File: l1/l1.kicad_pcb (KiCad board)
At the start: 2 copper layers, 113 parts, among them J201 Conn_01x10, SW201 SW_SPDT, U201 STM32F103CBTX, U202 CD74HC4067SM, U203 CD74HC4067SM, U204 TPS22917x, U205 ILD8150, Y201 8Mhz

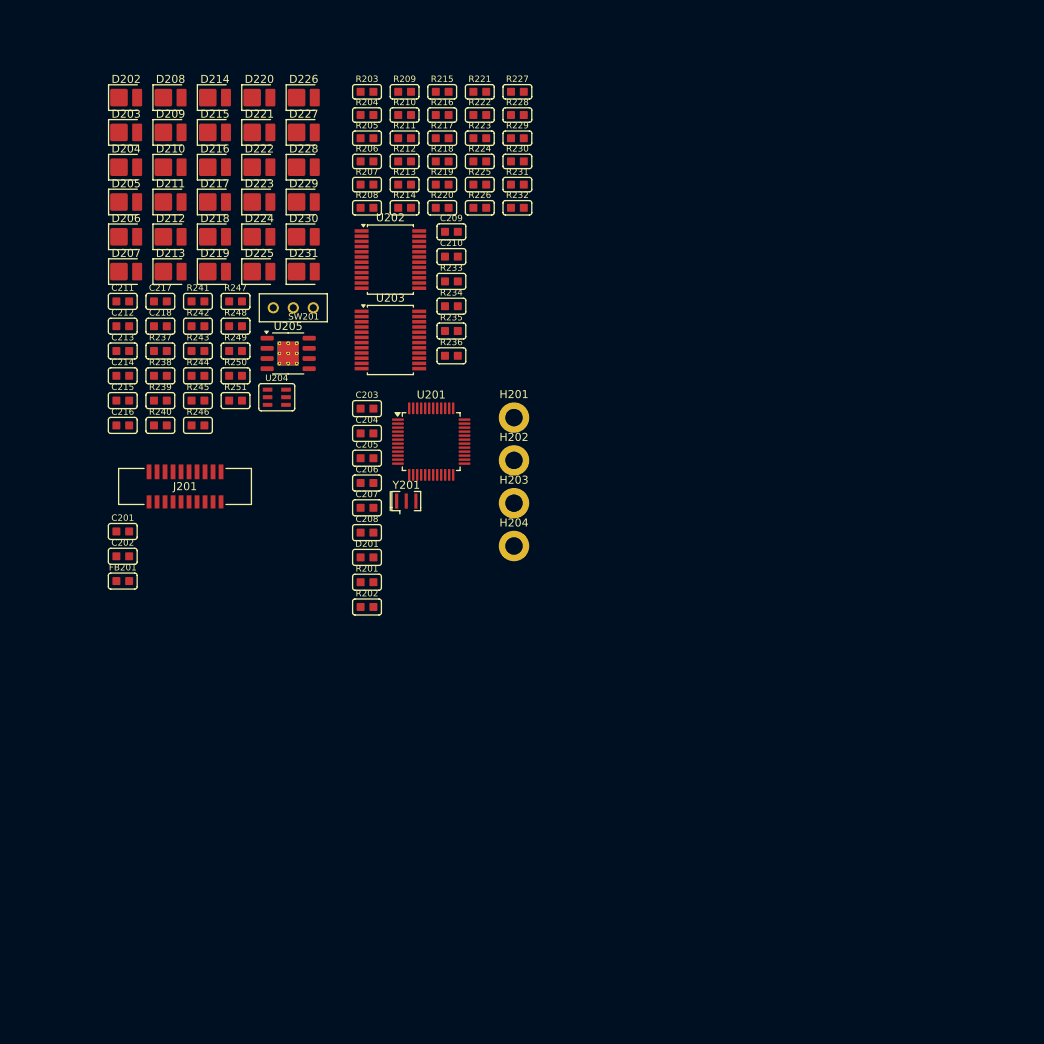
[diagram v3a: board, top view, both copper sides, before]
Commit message: Going to move to VNH
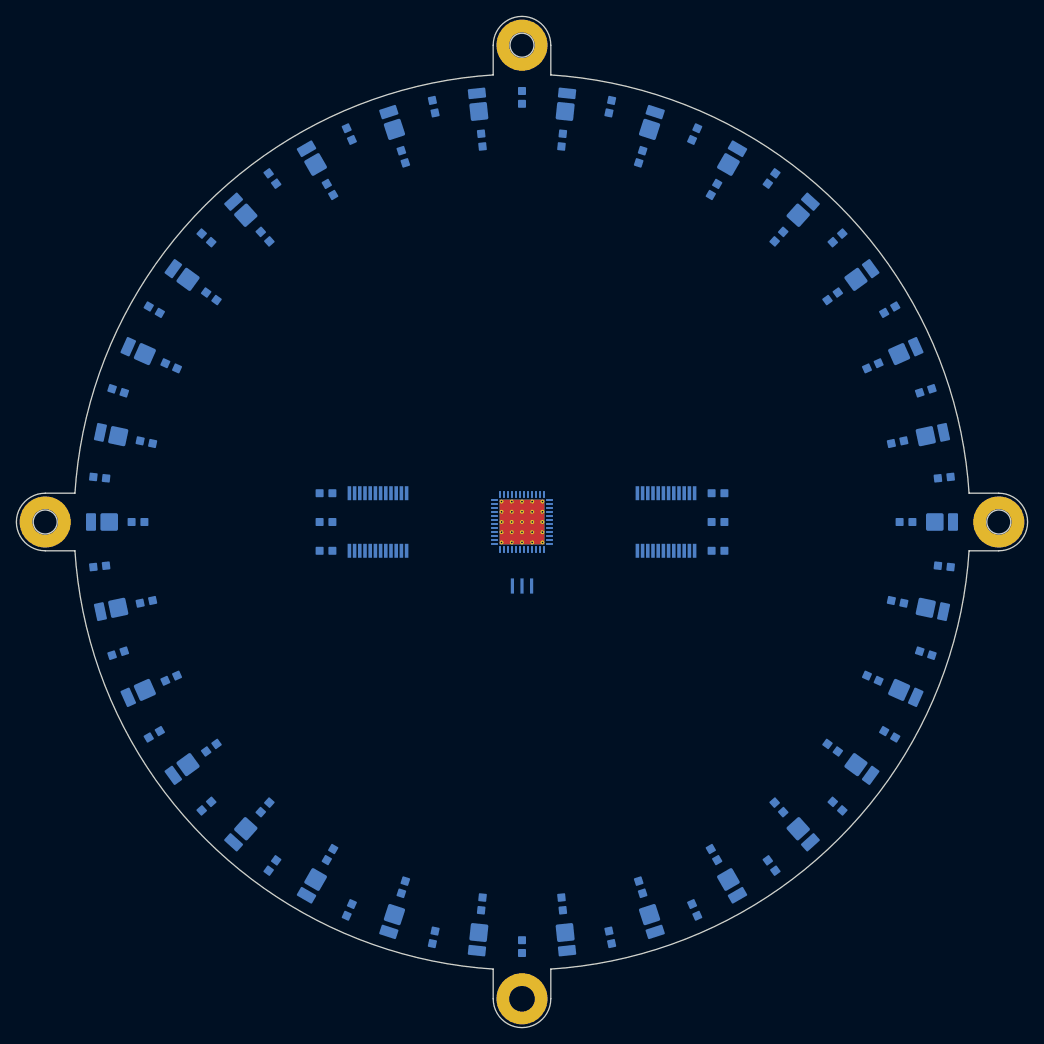
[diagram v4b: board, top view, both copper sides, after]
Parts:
- removed C201, C202, C203: 2u2, Library:cap0603
- removed C204, C205, C206, C207, C208, C211, C215, C218: 0u1, Library:cap0603
- removed C212: 10n, Library:cap0603
- removed C213: 10u, Library:cap0603
- removed C214, C216: 22u, Library:cap0603
- removed C217: 1u, Library:cap0603
- removed D201: RED, Library:led0603
- removed FB201: 100R, Library:fb0603
- removed J201: Conn_01x10, Library:526101071
- removed R201: R, Library:res0603
- removed R202: 1K, Library:res0603
- removed R237: 150, Library:res0603
- removed SW201: SW_SPDT, Library:SS12D00G3
- removed U204: TPS22917x, Library:SOT-23-6
- removed U205: ILD8150, Package_SO:Infineon_PG-DSO-8-27_3.9x4.9mm_EP2.65x3mm_ThermalVias
- added R252: R, Library:res0603, B.Cu at (202.2, 120.0)
- added R253: R, Library:res0603, B.Cu at (203.2, 110.0)
- added R254: R, Library:res0603, B.Cu at (202.2, 100.0)
- added R255: R, Library:res0603, B.Cu at (199.1, 90.5)
- added R256: R, Library:res0603, B.Cu at (194.0, 81.8)
- added R257: R, Library:res0603, B.Cu at (187.3, 74.3)
- added R258: R, Library:res0603, B.Cu at (179.2, 68.4)
- added R259: R, Library:res0603, B.Cu at (170.0, 64.3)
- added R260: R, Library:res0603, B.Cu at (160.2, 62.3)
- added R261: R, Library:res0603, B.Cu at (150.2, 62.3)
- added R262: R, Library:res0603, B.Cu at (140.4, 64.3)
- added R263: R, Library:res0603, B.Cu at (131.2, 68.4)
- added R264: R, Library:res0603, B.Cu at (123.1, 74.3)
- added R265: R, Library:res0603, B.Cu at (116.4, 81.8)
- added R266: R, Library:res0603, B.Cu at (111.3, 90.5)
- added R267: R, Library:res0603, B.Cu at (108.2, 100.0)
- C209, C210, D202, D203, D204, D205, D206, D207, D208, D209, D210, D211, D212, D213, D214, D215, D216, D217, D218, D219, D220, D221, D222, D223, D224, D225, D226, D227, D228, D229, D230, D231, R203, R204, R205, R206, R207, R208, R209, R210, R211, R212, R213, R214, R215, R216, R217, R218, R219, R220, R221, R222, R223, R224, R225, R226, R227, R228, R229, R230, R231, R232, R233, R234, R235, R236, R250, U202, U203, Y201: moved to B.Cu
- H201, H202, H203, H204: footprint MountingHole:MountingHole_2.2mm_M2_ISO14580_Pad -> MountingHole:MountingHole_3.2mm_M3_Pad
- R238, R239, R240, R241, R242, R243, R244, R245, R246: value 150 -> R; moved to B.Cu
- R247: value 100K -> R; moved to B.Cu
- R248: value 1 -> R; moved to B.Cu
- R249: value 10K -> R; moved to B.Cu
- R251: value 0.3 -> R; moved to B.Cu
- U201: value STM32F103CBTX -> STM32F103Cx; footprint Package_QFP:LQFP-48_7x7mm_P0.5mm -> Package_DFN_QFN:QFN-48-1EP_7x7mm_P0.5mm_EP5.6x5.6mm_ThermalVias; moved to B.Cu
- moved D214 116.5 mm to (197.7, 140.9), turned to -36 degrees
- moved D215 111.2 mm to (203.2, 131.4), turned to -24 degrees
- moved R203 108.6 mm to (155.2, 163.1), turned to 90 degrees
- moved D210 108.5 mm to (160.7, 162.2), turned to -84 degrees
- moved D211 108.2 mm to (171.4, 159.9), turned to -72 degrees
- moved D209 108.0 mm to (149.7, 162.2), turned to -96 degrees
- moved D212 107.3 mm to (181.4, 155.5), turned to -60 degrees
- moved R204 107.2 mm to (166.2, 161.9), turned to 102 degrees
- moved D208 106.6 mm to (139.0, 159.9), turned to -108 degrees
- moved D213 105.8 mm to (190.3, 149.0), turned to -48 degrees
- moved D216 105.4 mm to (206.6, 120.9), turned to -12 degrees
- moved R205 104.8 mm to (176.8, 158.5), turned to 114 degrees
- moved R206 101.5 mm to (186.4, 152.9), turned to 126 degrees
- moved D217 99.3 mm to (207.7, 110.0)
- moved R207 97.4 mm to (194.6, 145.5), turned to 138 degrees
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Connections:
- D202 pad 2: /Light Ring/LED/LED VIN -> Net-(D202-A)
- D203 pad 2: /Light Ring/LED/LED VIN -> Net-(D202-A)
- D204 pad 2: /Light Ring/LED/LED VIN -> Net-(D202-A)
- D205 pad 2: /Light Ring/LED/LED VIN -> Net-(D202-A)
- D206 pad 2: /Light Ring/LED/LED VIN -> Net-(D202-A)
- D207 pad 2: /Light Ring/LED/LED VIN -> Net-(D202-A)
- D208 pad 2: /Light Ring/LED/LED VIN -> Net-(D202-A)
- D209 pad 2: /Light Ring/LED/LED VIN -> Net-(D202-A)
- D210 pad 2: /Light Ring/LED/LED VIN -> Net-(D202-A)
- D211 pad 2: /Light Ring/LED/LED VIN -> Net-(D202-A)
- D212 pad 2: Net-(D202-K) -> Net-(D202-A)
- D213 pad 2: Net-(D203-K) -> Net-(D202-A)
- D214 pad 2: Net-(D204-K) -> Net-(D202-A)
- D215 pad 2: Net-(D205-K) -> Net-(D202-A)
- D216 pad 2: Net-(D206-K) -> Net-(D202-A)
- D217 pad 2: Net-(D207-K) -> Net-(D202-A)
- D218 pad 2: Net-(D208-K) -> Net-(D202-A)
- D219 pad 2: Net-(D209-K) -> Net-(D202-A)
- D220 pad 2: Net-(D210-K) -> Net-(D202-A)
- D221 pad 2: Net-(D211-K) -> Net-(D202-A)
- D222 pad 2: Net-(D212-K) -> Net-(D202-A)
- D223 pad 2: Net-(D213-K) -> Net-(D202-A)
- D224 pad 2: Net-(D214-K) -> Net-(D202-A)
- D225 pad 2: Net-(D215-K) -> Net-(D202-A)
- D226 pad 2: Net-(D216-K) -> Net-(D202-A)
- D227 pad 2: Net-(D217-K) -> Net-(D202-A)
- D228 pad 2: Net-(D218-K) -> Net-(D202-A)
- D229 pad 2: Net-(D219-K) -> Net-(D202-A)
- D230 pad 2: Net-(D220-K) -> Net-(D202-A)
- D231 pad 2: Net-(D221-K) -> Net-(D202-A)
- R238 pad 1: Net-(D223-K) -> Net-(D202-K)
- R238 pad 2: /Light Ring/LED/LED VOUT -> GNDREF
- R239 pad 1: Net-(D224-K) -> Net-(D203-K)
- R239 pad 2: /Light Ring/LED/LED VOUT -> GNDREF
- R240 pad 1: Net-(D225-K) -> Net-(D204-K)
- R240 pad 2: /Light Ring/LED/LED VOUT -> GNDREF
- R241 pad 1: Net-(D226-K) -> Net-(D205-K)
- R241 pad 2: /Light Ring/LED/LED VOUT -> GNDREF
- R242 pad 1: Net-(D227-K) -> Net-(D206-K)
- R242 pad 2: /Light Ring/LED/LED VOUT -> GNDREF
- R243 pad 1: Net-(D228-K) -> Net-(D207-K)
- R243 pad 2: /Light Ring/LED/LED VOUT -> GNDREF
- R244 pad 1: Net-(D229-K) -> Net-(D208-K)
- R244 pad 2: /Light Ring/LED/LED VOUT -> GNDREF
- R245 pad 1: Net-(D230-K) -> Net-(D209-K)
- R245 pad 2: /Light Ring/LED/LED VOUT -> GNDREF
- R246 pad 1: Net-(D231-K) -> Net-(D210-K)
- R246 pad 2: /Light Ring/LED/LED VOUT -> GNDREF
- R247 pad 1: Net-(U204-VOUT) -> Net-(D211-K)
- R247 pad 2: Net-(U204-QOD) -> GNDREF
- R248 pad 1: /Light Ring/LED/LED VOUT -> Net-(D212-K)
- R248 pad 2: Net-(R248-Pad2) -> GNDREF
- R249 pad 1: +3V3 FLIT -> Net-(D213-K)
- R249 pad 2: Net-(SW201-B) -> GNDREF
- R250 pad 1: Net-(SW201-B) -> Net-(D214-K)
- R250 pad 2: /Light Ring/LED/LED PWR -> GNDREF
- R251 pad 1: Net-(R248-Pad2) -> Net-(D215-K)
- U201 pad 10: LED DIM -> unconnected-(U201C-PA0-Pad10)
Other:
- board outline added: 126.4 x 126.4 mm

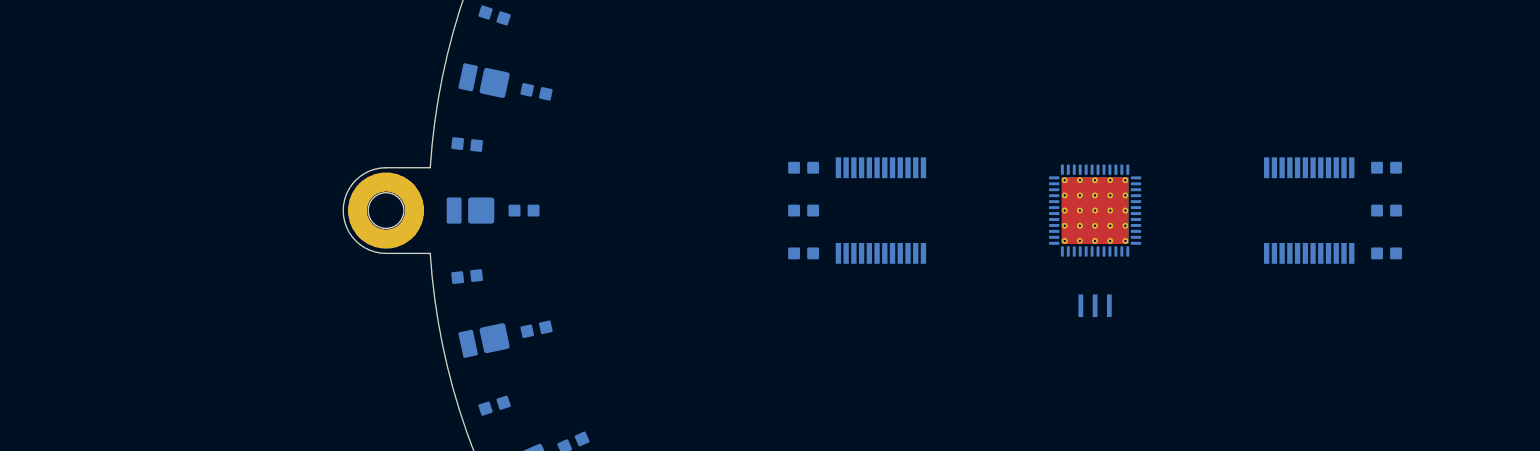
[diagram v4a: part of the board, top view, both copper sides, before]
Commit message: L1 - Left wiring
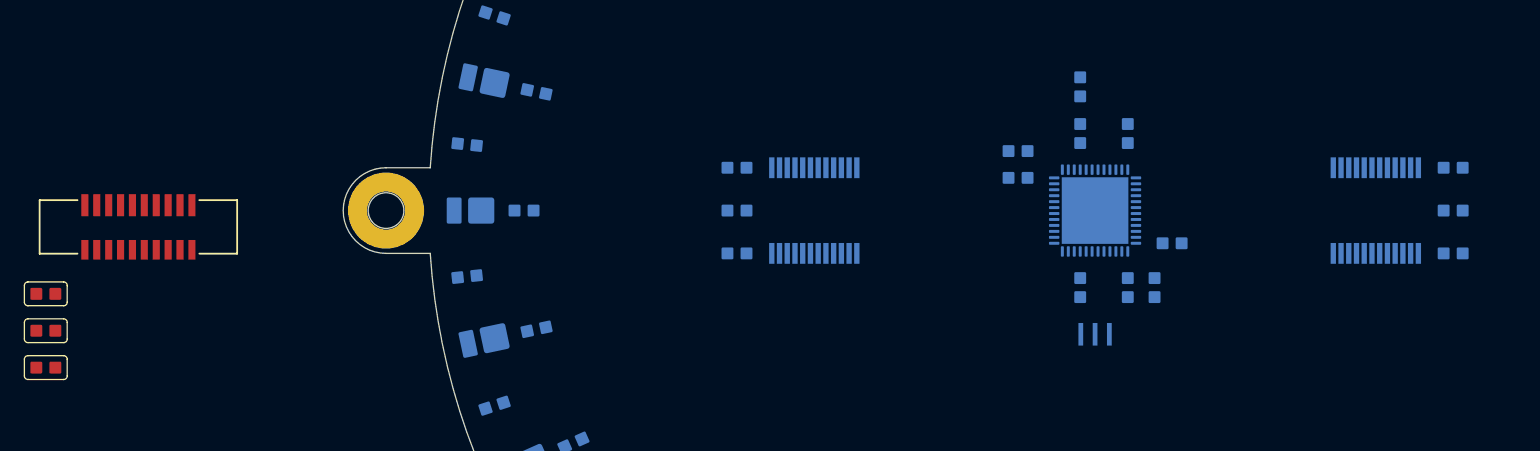
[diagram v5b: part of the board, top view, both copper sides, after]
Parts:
- removed R267: R, Library:res0603
- added C201: 2u2, Library:cap0603, F.Cu at (67.0, 117.0)
- added C202: 2u2, Library:cap0603, F.Cu at (67.0, 120.1)
- added C203: 2u2, Library:cap0603, B.Cu at (148.7, 105.0)
- added C204: 0u1, Library:cap0603, B.Cu at (157.9, 116.5)
- added C205: 0u1, Library:cap0603, B.Cu at (161.7, 112.8)
- added C206: 0u1, Library:cap0603, B.Cu at (157.9, 103.5)
- added C207: 0u1, Library:cap0603, B.Cu at (148.7, 107.2)
- added C208: 0u1, Library:cap0603, B.Cu at (153.9, 116.5)
- added D201: RED, Library:led0603, B.Cu at (153.9, 103.5)
- added FB201: 100R, Library:fb0603, F.Cu at (67.0, 123.2)
- added J201: Conn_01x10, Library:526101071, F.Cu at (74.8, 111.4)
- added R201: R, Library:res0603, B.Cu at (160.2, 116.5)
- added R202: 1K, Library:res0603, B.Cu at (153.9, 99.6)
- added R238: R, Library:res0603, B.Cu at (108.2, 120.0)
- U201: footprint Package_DFN_QFN:QFN-48-1EP_7x7mm_P0.5mm_EP5.6x5.6mm_ThermalVias -> Package_DFN_QFN:QFN-48-1EP_7x7mm_P0.5mm_EP5.6x5.6mm
- moved R256 10.0 mm to (187.3, 74.3), turned to -132 degrees
- moved R264 10.0 mm to (116.4, 81.8), turned to -36 degrees
- moved R241 10.0 mm to (123.1, 145.7), turned to 48 degrees
- moved R249 10.0 mm to (194.0, 138.2), turned to 144 degrees
- moved R244 10.0 mm to (150.2, 157.7), turned to 84 degrees
- moved R246 10.0 mm to (170.0, 155.7), turned to 108 degrees
- moved R259 10.0 mm to (160.2, 62.3), turned to -96 degrees
- moved R261 10.0 mm to (140.4, 64.3), turned to -72 degrees
- moved R239 10.0 mm to (111.3, 129.5), turned to 24 degrees
- moved R266 10.0 mm to (108.2, 100.0), turned to -12 degrees
- moved R251 10.0 mm to (202.2, 120.0), turned to 168 degrees
- moved R254 10.0 mm to (199.1, 90.5), turned to -156 degrees
- moved R243 10.0 mm to (140.4, 155.7), turned to 72 degrees
- moved R262 10.0 mm to (131.2, 68.4), turned to -60 degrees
- moved R247 10.0 mm to (179.2, 151.6), turned to 120 degrees
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- renumbered R238 to R237
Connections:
- net Net-(D202-A) renamed +3V3_FILT
- R239 pad 1: Net-(D203-K) -> Net-(D204-K)
- R240 pad 1: Net-(D204-K) -> Net-(D205-K)
- R241 pad 1: Net-(D205-K) -> Net-(D206-K)
- R242 pad 1: Net-(D206-K) -> Net-(D207-K)
- R243 pad 1: Net-(D207-K) -> Net-(D208-K)
- R244 pad 1: Net-(D208-K) -> Net-(D209-K)
- R245 pad 1: Net-(D209-K) -> Net-(D210-K)
- R246 pad 1: Net-(D210-K) -> Net-(D211-K)
- R247 pad 1: Net-(D211-K) -> Net-(D212-K)
- R248 pad 1: Net-(D212-K) -> Net-(D213-K)
- R249 pad 1: Net-(D213-K) -> Net-(D214-K)
- R250 pad 1: Net-(D214-K) -> Net-(D215-K)
- R251 pad 1: Net-(D215-K) -> Net-(D216-K)
- R252 pad 1: Net-(D216-K) -> Net-(D217-K)
- R253 pad 1: Net-(D217-K) -> Net-(D218-K)
- R254 pad 1: Net-(D218-K) -> Net-(D219-K)
- R255 pad 1: Net-(D219-K) -> Net-(D220-K)
- R256 pad 1: Net-(D220-K) -> Net-(D221-K)
- R257 pad 1: Net-(D221-K) -> Net-(D222-K)
- R258 pad 1: Net-(D222-K) -> Net-(D223-K)
- R259 pad 1: Net-(D223-K) -> Net-(D224-K)
- R260 pad 1: Net-(D224-K) -> Net-(D225-K)
- R261 pad 1: Net-(D225-K) -> Net-(D226-K)
- R262 pad 1: Net-(D226-K) -> Net-(D227-K)
- R263 pad 1: Net-(D227-K) -> Net-(D228-K)
- R264 pad 1: Net-(D228-K) -> Net-(D229-K)
- R265 pad 1: Net-(D229-K) -> Net-(D230-K)
- R266 pad 1: Net-(D230-K) -> Net-(D231-K)

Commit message: Fab
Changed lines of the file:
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@@
 		(fp_arc
 			(start -1.5 1)
-			(mid -1.712133 0.912132)
+			(mid -1.712133 0.912133)
 			(end -1.8 0.699999)
 			(stroke
@@
 		(fp_arc
 			(start -1.5 1)
-			(mid -1.712131 0.912132)
+			(mid -1.712131 0.912131)
 			(end -1.8 0.7)
 			(stroke
@@
 		(fp_arc
 			(start -1.8 -0.7)
-			(mid -1.712131 -0.912132)
+			(mid -1.712131 -0.912131)
 			(end -1.5 -1)
 			(stroke
@@
 		(fp_arc
 			(start -1.5 1)
-			(mid -1.712131 0.912132)
+			(mid -1.712132 0.912131)
 			(end -1.8 0.7)
 			(stroke
@@
 		)
 		(pad "1" smd roundrect
-			(at -0.8 0 84)
+			(at -0.800001 0 84)
 			(size 1 1)
 			(layers "B.Cu" "B.Paste" "B.Mask")
@@
 		)
 		(pad "2" smd roundrect
-			(at 0.8 0 84)
+			(at 0.800001 0 84)
 			(size 1 1)
 			(layers "B.Cu" "B.Paste" "B.Mask")
@@
 		(fp_arc
 			(start -1.5 1)
-			(mid -1.712132 0.912131)
+			(mid -1.712131 0.912131)
 			(end -1.8 0.7)
 			(stroke
@@
 		(fp_arc
 			(start -1.8 -0.7)
-			(mid -1.712132 -0.912133)
+			(mid -1.712133 -0.912133)
 			(end -1.5 -1)
 			(stroke
@@
 		(fp_arc
 			(start -1.8 -0.7)
-			(mid -1.712131 -0.912132)
+			(mid -1.712132 -0.912131)
 			(end -1.5 -1)
 			(stroke
@@
 		)
 		(pad "1" smd roundrect
-			(at -0.8 0 96)
+			(at -0.800001 0 96)
 			(size 1 1)
 			(layers "B.Cu" "B.Paste" "B.Mask")
@@
 		)
 		(pad "2" smd roundrect
-			(at 0.8 0 96)
+			(at 0.800001 0 96)
 			(size 1 1)
 			(layers "B.Cu" "B.Paste" "B.Mask")
@@
 		(fp_arc
 			(start -1.8 -0.6)
-			(mid -1.712133 -0.812134)
+			(mid -1.712134 -0.812134)
 			(end -1.5 -0.9)
 			(stroke
@@
 		(fp_arc
 			(start -1.8 -0.7)
-			(mid -1.712132 -0.912133)
+			(mid -1.712133 -0.912133)
 			(end -1.5 -1)
 			(stroke
@@
 		(fp_arc
 			(start -1.5 1)
-			(mid -1.712132 0.912131)
+			(mid -1.712131 0.912131)
 			(end -1.8 0.7)
 			(stroke
@@
 		(fp_arc
 			(start -1.5 1)
-			(mid -1.712131 0.912132)
+			(mid -1.712132 0.912131)
 			(end -1.8 0.7)
 			(stroke
@@
 		(fp_arc
 			(start -1.8 -0.7)
-			(mid -1.712131 -0.912132)
+			(mid -1.712131 -0.912131)
 			(end -1.5 -1)
 			(stroke
@@
 		)
 		(pad "1" smd roundrect
-			(at -0.8 0 264)
+			(at -0.800001 0 264)
 			(size 1 1)
 			(layers "B.Cu" "B.Paste" "B.Mask")
@@
 		)
 		(pad "2" smd roundrect
-			(at 0.8 0 264)
+			(at 0.800001 0 264)
 			(size 1 1)
 			(layers "B.Cu" "B.Paste" "B.Mask")
@@
 		(fp_arc
 			(start -1.8 -0.6)
-			(mid -1.712133 -0.812134)
+			(mid -1.712134 -0.812134)
 			(end -1.5 -0.9)
 			(stroke
@@
 		(fp_arc
 			(start -1.5 1)
-			(mid -1.712131 0.912132)
+			(mid -1.712131 0.912131)
 			(end -1.8 0.7)
 			(stroke
@@
 		(fp_arc
 			(start -1.799999 -0.7)
-			(mid -1.712132 -0.912131)
+			(mid -1.712133 -0.912132)
 			(end -1.5 -1)
 			(stroke
@@
 		(fp_arc
 			(start -1.799999 -0.7)
-			(mid -1.712132 -0.912131)
+			(mid -1.712133 -0.912132)
 			(end -1.5 -1)
 			(stroke
@@
 		(at 203.2 110 180)
 		(property "Reference" "R252"
-			(at 0 1.700001 360)
+			(at 0 1.700001 0)
 			(layer "B.SilkS")
 			(hide yes)
@@
 		(fp_arc
 			(start -1.8 -0.7)
-			(mid -1.712131 -0.912132)
+			(mid -1.712132 -0.912131)
 			(end -1.5 -1)
 			(stroke
@@
 		)
 		(pad "1" smd roundrect
-			(at -0.8 0 276)
+			(at -0.800001 0 276)
 			(size 1 1)
 			(layers "B.Cu" "B.Paste" "B.Mask")
@@
 		)
 		(pad "2" smd roundrect
-			(at 0.8 0 276)
+			(at 0.800001 0 276)
 			(size 1 1)
 			(layers "B.Cu" "B.Paste" "B.Mask")
@@
 		(fp_arc
 			(start -1.5 1)
-			(mid -1.712133 0.912132)
+			(mid -1.712133 0.912133)
 			(end -1.8 0.699999)
 			(stroke
@@
 	)
 	(gr_arc
+		(start 206.43817 93.35171)
+		(mid 104.903355 129.307073)
+		(end 204.417261 88.087063)
+		(stroke
+			(width 1)
+			(type default)
+		)
+		(layer "B.Cu")
+	)
+	(gr_arc
 		(start 211.084165 113.599999)
 		(mid 194.797979 149.597979)
@@
 		(layer "Edge.Cuts")
 	)
-	(zone
-		(net 1)
-		(net_name "+3V3")
-		(layer "B.Cu")
-		(name "$teardrop_padvia$")
-		(hatch full 0.1)
-		(priority 30000)
-		(attr
-			(teardrop
-				(type padvia)
-			)
-		)
-		(connect_pads yes
-			(clearance 0)
-		)
-		(min_thickness 0.0254)
-		(filled_areas_thickness no)
-		(fill yes
-			(thermal_gap 0.5)
-			(thermal_bridge_width 0.5)
-			(island_removal_mode 1)
-			(island_area_min 10)
-		)
-		(polygon
-			(pts
-				(xy 160.2 112.875) (xy 160.256173 112.87641) (xy 160.312346 112.882338) (xy 160.368519 112.892783)
-				(xy 160.424692 112.907745) (xy 160.480866 112.927225) (xy 160.537039 112.951223) (xy 160.593212 112.979738)
-				(xy 160.649385 113.01277) (xy 160.705558 113.05032) (xy 160.761732 113.092388) (xy 161.201 112.6)
-				(xy 160.706254 112.168555) (xy 160.655628 112.237204) (xy 160.605003 112.300742) (xy 160.554377 112.359167)
-				(xy 160.503752 112.41248) (xy 160.453127 112.460681) (xy 160.402501 112.503769) (xy 160.351876 112.541745)
-				(xy 160.30125 112.574609) (xy 160.250625 112.60236) (xy 160.2 112.625)
-			)
-		)
-	)
 	(group ""

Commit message: l1 temp
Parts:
- moved J201 89.0 mm to (155.5, 73.9)
- turned C210 to 0 degrees
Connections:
- D202 pad 2: +3V3_FILT -> +3V3
- D203 pad 2: +3V3_FILT -> +3V3
- D204 pad 2: +3V3_FILT -> +3V3
- D205 pad 2: +3V3_FILT -> +3V3
- D206 pad 2: +3V3_FILT -> +3V3
- D207 pad 2: +3V3_FILT -> +3V3
- D208 pad 2: +3V3_FILT -> +3V3
- D209 pad 2: +3V3_FILT -> +3V3
- D210 pad 2: +3V3_FILT -> +3V3
- D211 pad 2: +3V3_FILT -> +3V3
- D212 pad 2: +3V3_FILT -> +3V3
- D213 pad 2: +3V3_FILT -> +3V3
- D214 pad 2: +3V3_FILT -> +3V3
- D215 pad 2: +3V3_FILT -> +3V3
- D216 pad 2: +3V3_FILT -> +3V3
- D217 pad 2: +3V3_FILT -> +3V3
- D218 pad 2: +3V3_FILT -> +3V3
- D219 pad 2: +3V3_FILT -> +3V3
- D220 pad 2: +3V3_FILT -> +3V3
- D221 pad 2: +3V3_FILT -> +3V3
- D222 pad 2: +3V3_FILT -> +3V3
- D223 pad 2: +3V3_FILT -> +3V3
- D224 pad 2: +3V3_FILT -> +3V3
- D225 pad 2: +3V3_FILT -> +3V3
- D226 pad 2: +3V3_FILT -> +3V3
- D227 pad 2: +3V3_FILT -> +3V3
- D228 pad 2: +3V3_FILT -> +3V3
- D229 pad 2: +3V3_FILT -> +3V3
- D230 pad 2: +3V3_FILT -> +3V3
- D231 pad 2: +3V3_FILT -> +3V3
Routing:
- net Net-(U203-~{E}): track 0.00 -> 11.2 mm
- net +3V3: track 0.00 -> 4.25 mm
- net /Light Ring/MUX/M2: track 0.00 -> 2.12 mm
- added copper zone on B.Cu, net GNDREF
- added copper zone on F.Cu, net GNDREF
